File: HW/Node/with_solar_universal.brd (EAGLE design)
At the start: 88.9 x 53.3 mm, 27 parts, among them U1 MS560702BA03-50, U2 HDC2080DMBR, U3 RFM69HW, U4 LTC3106, X1 734120110

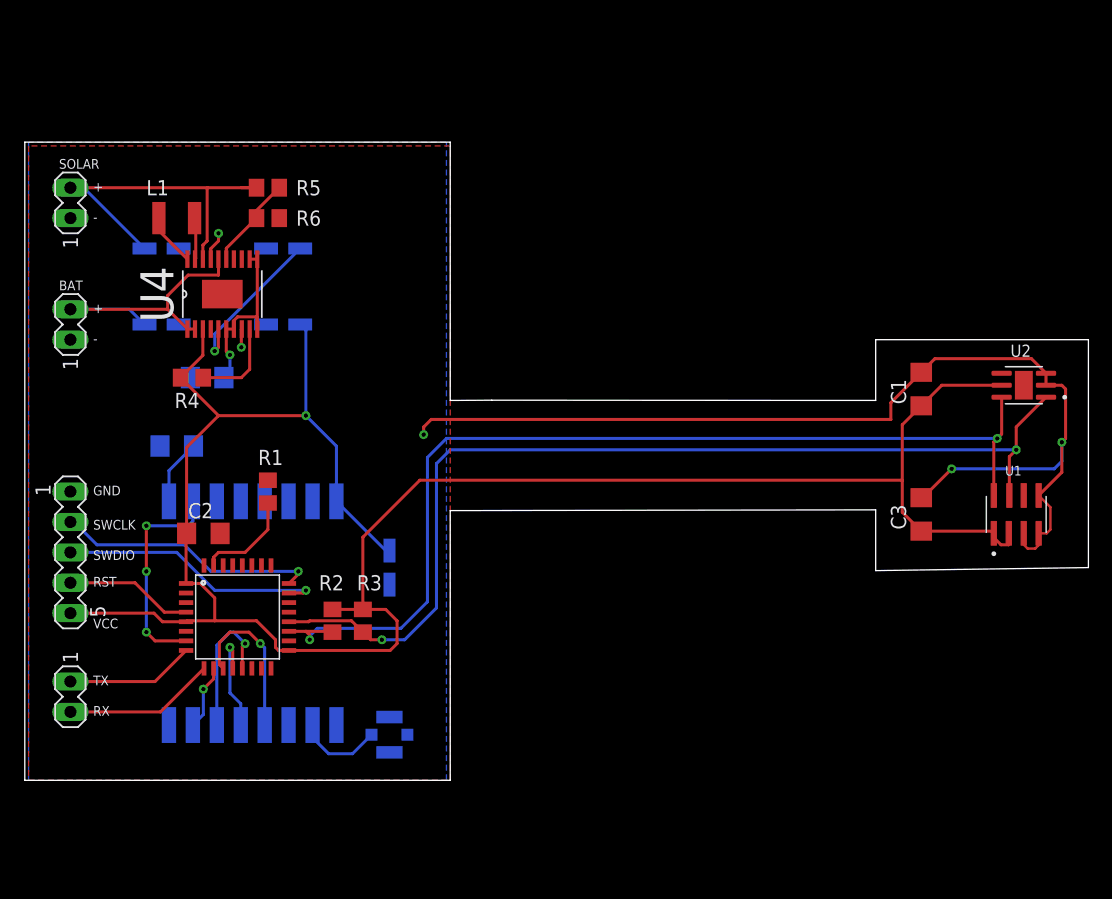
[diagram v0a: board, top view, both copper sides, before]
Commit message: HW: Update node schematic and board
Signed-off-by: Ales Musil <aedvin1@gmail.com>
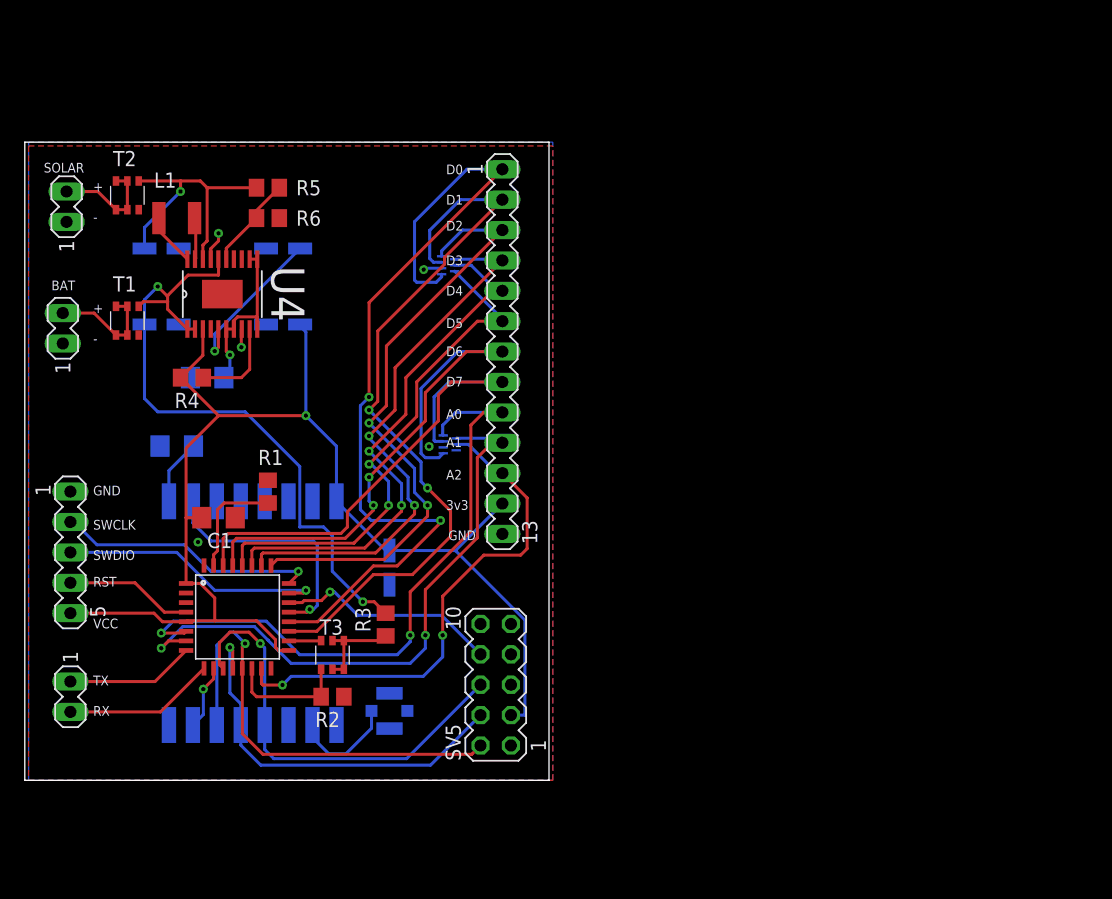
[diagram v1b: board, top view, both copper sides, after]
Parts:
- removed C10, C9: 47u, rcl:UD-4X5,8_NICHICON
- removed U1: MS560702BA03-50, MS560702BA03-50:SON125P300X500X100-8N
- removed U2: HDC2080DMBR, HDC2080DMBR2:SON100P300X300X80-7N
- added IC1, IC2: PUSB3FR6, esd:DFN2111-7
- added SV5: (no value), con-lstb:MA05-2
- added SV6: (no value), con-lstb:MA13-1
- added T1, T2: RTQ035P02HZG, dp:SOT457R_PHILIPS
- added T3: (no value), dp:SOT457R_PHILIPS
- C2: value 100n -> 10u; device rcl:C1206 -> rcl:UD-4X5,8_NICHICON
- C3, C7: value 100n -> 47u; device rcl:C1206 -> rcl:UD-4X5,8_NICHICON
- C4: value 10u -> 100n; device rcl:UD-4X5,8_NICHICON -> rcl:C1206
- R2: value 10k -> 8k
- R3: value 10k -> 2k
- moved C1 59.7 mm to (16.2, 22.0), turned to 0 degrees
- moved C3 55.7 mm to (21.6, 38.1), flipped to the bottom, turned to 180 degrees
- moved C4 20.5 mm to (12.7, 27.9), turned to 0 degrees
- moved C2 15.8 mm to (30.5, 17.8), flipped to the bottom, turned to 90 degrees
- moved C5 12.0 mm to (11.4, 44.5), turned to 0 degrees
- moved SV2 10.5 mm to (3.17, 39.1)
- moved C7 10.2 mm to (11.4, 38.1)
- moved SV4 9.85 mm to (3.49, 49.2)
- moved R2 6.35 mm to (25.7, 6.99), turned to 180 degrees
- moved X1 1.99 mm to (30.5, 5.80)
- moved R3 1.93 mm to (30.2, 13.0)
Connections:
- new net A0: IC2.4, STM32L031K6_1.6, SV6.9
- new net A1: IC2.5, STM32L031K6_1.7, SV6.10
- new net A2: IC2.6, STM32L031K6_1.15, SV6.11
- new net BAT_ADC: R2.2, STM32L031K6_1.14, T3.4
- new net BAT_SW: STM32L031K6_1.18, T3.3
- new net D2: IC1.4, STM32L031K6_1.25, SV6.3
- new net D3: IC1.5, STM32L031K6_1.26, SV6.4
- new net D4: IC1.6, STM32L031K6_1.27, SV6.5
- new net D5: IC1.7, STM32L031K6_1.28, SV6.6
- new net D6: IC2.1, STM32L031K6_1.29, SV6.7
- new net D7: IC2.3, STM32L031K6_1.30, SV6.8
- new net N$19: R3.1, T3.1, T3.2, T3.5, T3.6
- new net SPI_NSS2: STM32L031K6_1.22, SV5.8
- new net T1: SV2.2, T1.1, T1.2, T1.5, T1.6
- new net T2: SV4.2, T2.1, T2.2, T2.5, T2.6
- net BAT_IN: now also C7.+, R3.2, T1.4; no longer C9.+, SV4.2
- net GND: now also C2.-, C3.-, C4.2, C7.-, IC1.2, IC2.2, R2.1, SV5.1, SV6.13, T1.3, T2.3; no longer C10.-, C2.2, C3.2, C4.-, C7.2, C9.-, U1.3, U1.4, U1.5, U2.2, U2.3
- net I2C_SCL: now also IC1.3, SV6.2; no longer R2.1, U1.8, U2.6
- net I2C_SDA: now also IC1.1, SV6.1; no longer R3.1, U1.7, U2.1
- net N$10: now also C4.1; no longer C7.1
- net RFM_INT: now also STM32L031K6_1.21; no longer STM32L031K6_1.7
- net SOLAR_IN: now also C5.+, T2.4; no longer C10.+, SV2.2
- net SPI_MISO: now also SV5.4
- net SPI_MOSI: now also SV5.2
- net SPI_SCK: now also SV5.6
- net VCC: now also C2.+, C3.+, SV5.3, SV6.12; no longer C2.1, C3.1, C4.+, C5.+, R2.2, R3.2, U1.1, U1.2, U2.5
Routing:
- net GND: track 95.3 -> 5.51 mm
- net VCC: track 177.0 -> 108.5 mm
- net A0: track 0.00 -> 54.6 mm, vias 0 -> 2
- net D2: track 0.00 -> 51.6 mm, vias 0 -> 2
- net A1: track 0.00 -> 51.3 mm, vias 0 -> 2
- net D6: track 0.00 -> 50.3 mm, vias 0 -> 2
- net D3: track 0.00 -> 46.5 mm, vias 0 -> 2
- net D4: track 0.00 -> 44.6 mm, vias 0 -> 2
- net D7: track 0.00 -> 43.7 mm
- net D5: track 0.00 -> 43.3 mm, vias 0 -> 2
- net A2: track 0.00 -> 43.2 mm, vias 0 -> 2
- net BAT_IN: track 25.3 -> 56.2 mm, vias 0 -> 2
- net SPI_MOSI: track 12.1 -> 38.4 mm
- net SPI_MISO: track 8.72 -> 32.9 mm
- net SPI_SCK: track 13.4 -> 36.4 mm
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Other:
- board size 88.9 x 53.3 mm -> 43.8 x 53.3 mm
- board text added: "3v3"
- board text added: "A0"
- board text added: "A1"
- board text added: "A2"
- board text added: "D0"
- board text added: "D1"
- board text added: "D2"
- board text added: "D3"
- board text added: "D4"
- board text added: "D5"
- board text added: "D6"
- board text added: "D7"

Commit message: HW: Update node schematic and board
- Use different input protection.
- Add current limiting resistor.
- Add AAA battery holder.

Signed-off-by: Ales Musil <aedvin1@gmail.com>
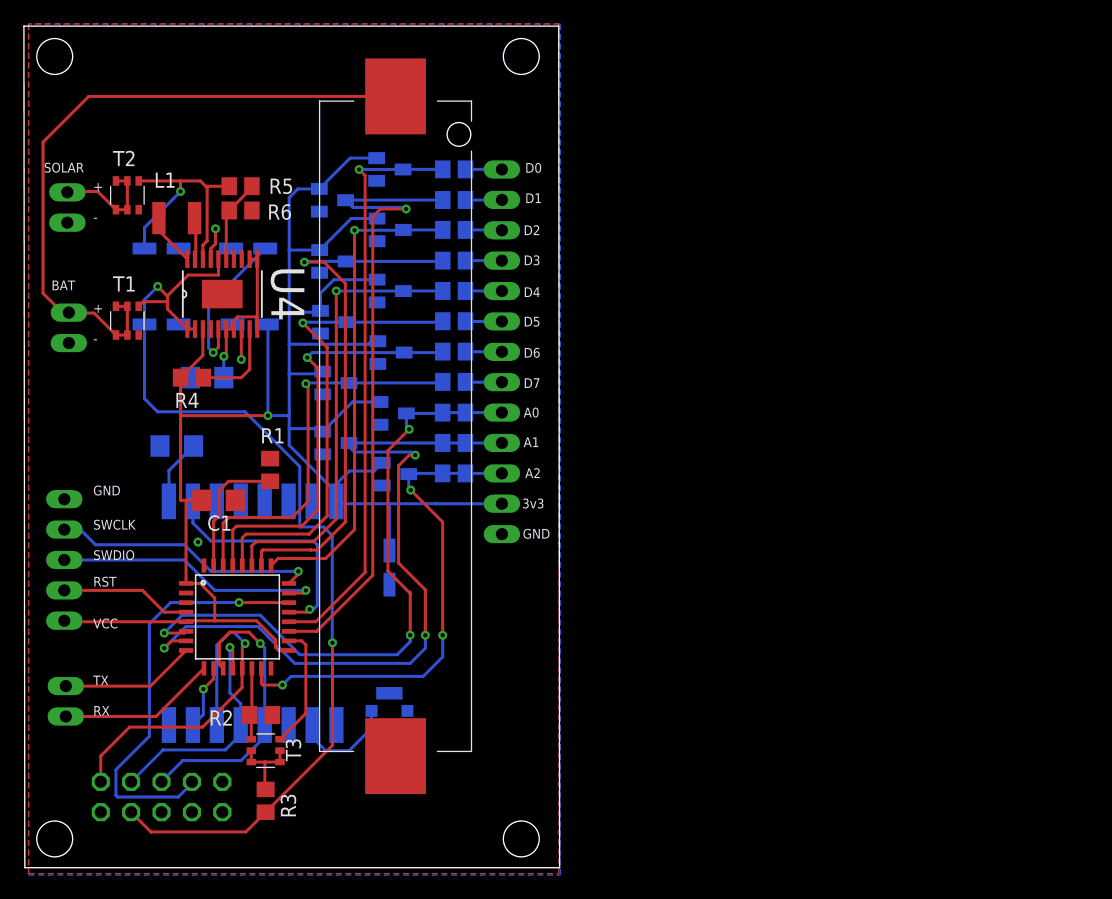
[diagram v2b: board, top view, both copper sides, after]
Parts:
- removed IC1, IC2: PUSB3FR6, esd:DFN2111-7
- removed SV1: PROG, con-lstb:MA05-1
- removed SV2: BAT, dp:MA02-1
- removed SV3: UART, dp:MA02-1
- removed SV4: SOLAR, dp:MA02-1
- removed SV5: (no value), con-lstb:MA05-2
- removed SV6: (no value), con-lstb:MA13-1
- added D1, D10, D11, D2, D3, D4, D5, D6, D7, D8, D9: BAS70-04, nxp_60:SOT23
- added J1: 1076, 1076:1076
- added R10, R11, R12, R13, R14, R7, R8, R9: 300R, rcl:R0805
- added U$1, U$2, U$3: SJ-C, dp:R0805
- added U$4, U$5, U$6: MA02-1, dp:MA02-1
- added U$7: MA05-1, dp:MA05-1
- added U$8: MA05-2, dp:MA05-2
- added U$9: MA13-1, dp:MA13-1
- moved R3 17.8 mm to (20.1, -1.71), turned to 270 degrees
- moved T3 9.76 mm to (20.1, 2.48), turned to 90 degrees
- moved R2 6.16 mm to (19.7, 5.46)
- moved C6 2.92 mm to (18.7, 44.5)
- moved C3 2.79 mm to (18.8, 38.1)
- moved R6 2.37 mm to (18.0, 47.6)
- moved R5 2.29 mm to (18.0, 49.7)
- moved R1 1.82 mm to (20.5, 25.9)
- moved C1 1.45 mm to (16.2, 23.4)
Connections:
- new net N$11: R9.1, U$9.3
- new net N$12: R10.1, U$9.4
- new net N$13: R11.1, U$9.5
- new net N$14: R12.1, U$9.6
- new net N$15: R13.1, U$9.7
- new net N$16: R14.1, U$9.8
- new net N$17: U$1.2, U$9.9
- new net N$18: U$2.2, U$9.10
- new net N$20: U$3.2, U$9.11
- new net N$8: R7.1, U$9.1
- new net N$9: R8.1, U$9.2
- net A0: now also D9.3, U$1.1; no longer IC2.4, SV6.9
- net A1: now also D10.3, U$2.1; no longer IC2.5, SV6.10
- net A2: now also D11.3, U$3.1; no longer IC2.6, SV6.11
- net BAT_IN: now also U$8.3
- net D2: now also D3.3, R9.2; no longer IC1.4, SV6.3
- net D3: now also D4.3, R10.2; no longer IC1.5, SV6.4
- net D4: now also D5.3, R11.2; no longer IC1.6, SV6.5
- net D5: now also D6.3, R12.2; no longer IC1.7, SV6.6
- net D6: now also D7.3, R13.2; no longer IC2.1, SV6.7
- net D7: now also D8.3, R14.2; no longer IC2.3, SV6.8
- net GND: now also D1.1, D10.1, D11.1, D2.1, D3.1, D4.1, D5.1, D6.1, D7.1, D8.1, D9.1, J1.2, U$4.1, U$5.1, U$7.1, U$8.1, U$9.13; no longer IC1.2, IC2.2, SV1.1, SV2.1, SV4.1, SV5.1, SV6.13
- net I2C_SCL: now also D2.3, R8.2; no longer IC1.3, SV6.2
- net I2C_SDA: now also D1.3, R7.2; no longer IC1.1, SV6.1
- net NRST: now also U$7.4; no longer SV1.4
- net SPI_MISO: now also U$8.4; no longer SV5.4
- net SPI_MOSI: now also U$8.2; no longer SV5.2
- net SPI_NSS2: now also U$8.8; no longer SV5.8
- net SPI_SCK: now also U$8.6; no longer SV5.6
- net SWCLK: now also U$7.2; no longer SV1.2
- net SWDIO: now also U$7.3; no longer SV1.3
- net T1: now also J1.1, U$4.2; no longer SV2.2
- net T2: now also U$5.2; no longer SV4.2
- net UART_RX: now also U$6.2; no longer SV3.2
- net UART_TX: now also U$6.1; no longer SV3.1
- net VCC: now also D1.2, D10.2, D11.2, D2.2, D3.2, D4.2, D5.2, D6.2, D7.2, D8.2, D9.2, U$7.5, U$9.12; no longer SV1.5, SV5.3, SV6.12
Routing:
- net VCC: track 108.5 -> 162.3 mm
- net T1: track 9.51 -> 55.5 mm
- net BAT_IN: track 56.2 -> 85.4 mm
- net I2C_SDA: track 73.5 -> 49.0 mm, vias 2 -> 1
- net SPI_NSS2: track 18.5 -> 34.9 mm
- net D6: track 50.3 -> 35.4 mm, vias 2 -> 1
- net SPI_MISO: track 32.9 -> 20.3 mm
- net SPI_SCK: track 36.4 -> 24.6 mm
- net D2: track 51.6 -> 40.6 mm, vias 2 -> 1
- net D7: track 43.7 -> 32.8 mm, vias 0 -> 1
- net SPI_MOSI: track 38.4 -> 30.0 mm
- net BAT_SW: track 2.70 -> 10.3 mm
- net I2C_SCL: track 63.0 -> 55.5 mm, vias 2 -> 1
- net D4: track 44.6 -> 37.6 mm, vias 2 -> 1
- net A1: track 51.3 -> 58.4 mm, vias 2 -> 3
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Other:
- board size 43.8 x 53.3 mm -> 44.8 x 70.3 mm
